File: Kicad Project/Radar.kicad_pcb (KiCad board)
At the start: 2 copper layers, 104.1 x 101.6 mm, 48 parts, among them U1 GALI-1+, U10 GALI-2+, U11 BandpassFilter, U2 MCA1-85L+, U3 BandpassFilter, U4 LMV751, U5 LMV751, U6 GALI-2+, U7 RMK-3-93+, U8 GALI-2+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

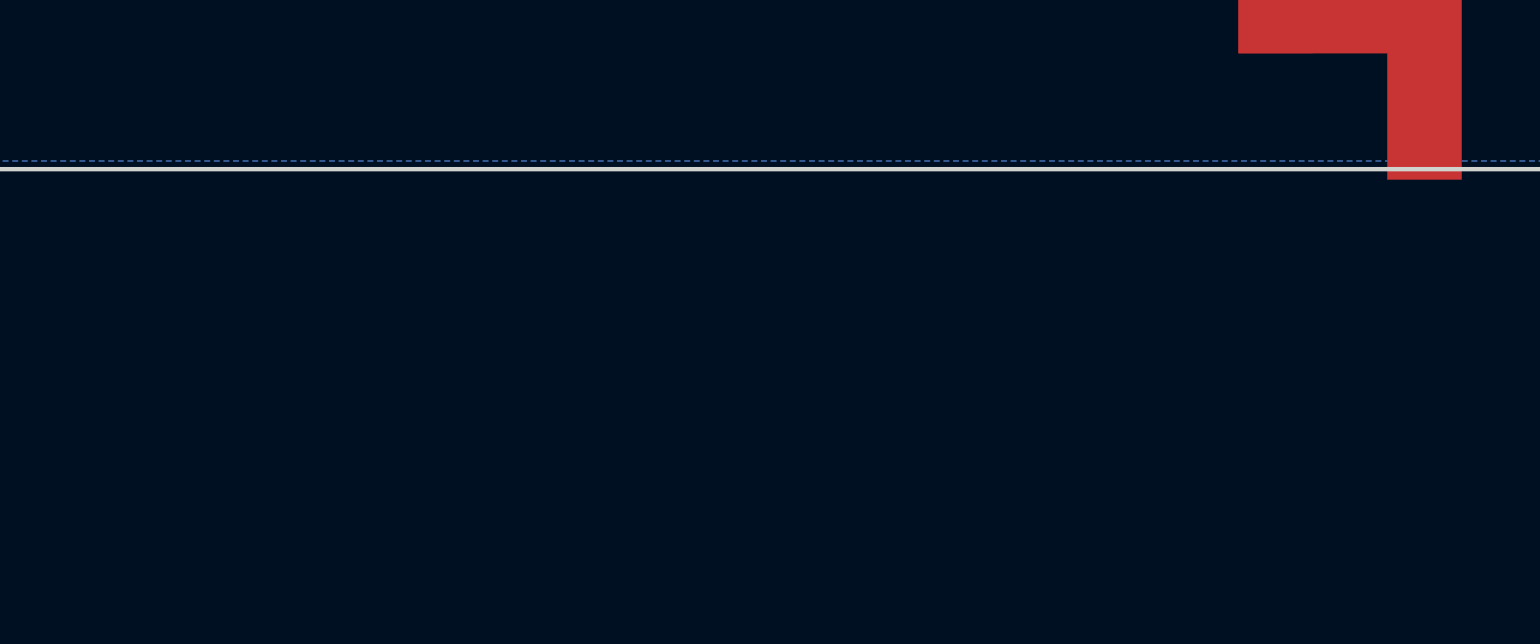
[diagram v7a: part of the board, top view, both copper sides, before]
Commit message: added antennas to pcb
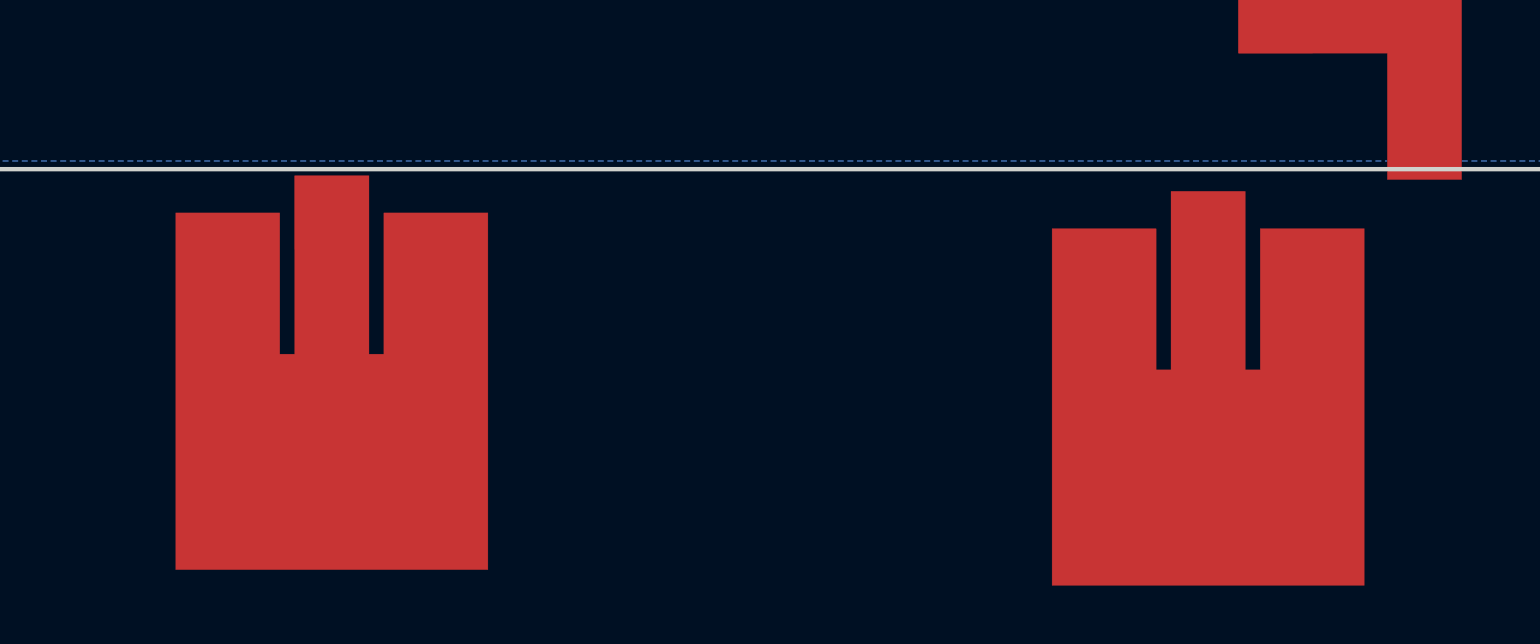
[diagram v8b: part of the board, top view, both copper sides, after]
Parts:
- added U13: Antenna111, RadarComponents:patch58, F.Cu at (116.1, 187.3)
- added U14: Antenna111, RadarComponents:patch58, F.Cu at (146.1, 187.9)
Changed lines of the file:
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@@
     (tracks 61)
     (zones 0)
-    (modules 48)
-    (nets 42)
+    (modules 50)
+    (nets 44)
   )
   (page A4)
@@
   (net 40 "Net-(C4-Pad1)")
   (net 41 "Net-(U3-Pad1)")
+  (net 42 "Net-(U13-Pad1)")
+  (net 43 "Net-(U14-Pad1)")
   (net_class Default "This is the default net class."
     (clearance 0.2)
@@
     (add_net "Net-(R6-Pad2)")
     (add_net "Net-(U11-Pad2)")
+    (add_net "Net-(U13-Pad1)")
+    (add_net "Net-(U14-Pad1)")
     (add_net "Net-(U3-Pad1)")
     (add_net "Net-(VCO1-Pad4)")
@@
       (net 41 "Net-(U3-Pad1)"))
   )
+  (module RadarComponents:patch58 (layer F.Cu)
+    (at 116.1034 187.3377 270)
+    (fp_text reference U13 (at -5.5372 -8.7122 270) (layer F.SilkS) hide
+      (effects (font (thickness 0.3)))
+    )
+    (fp_text value Antenna111 (at 1.0414 -8.636 270) (layer F.SilkS) hide
+      (effects (font (thickness 0.3)))
+    )
+    (fp_poly (pts (xy 4.148667 3.217333) (xy -8.043333 3.217333) (xy -8.043333 -0.338667) (xy -3.217333 -0.338667)
+      (xy -3.217333 -0.846667) (xy -9.313333 -0.846667) (xy -9.313333 -3.386667) (xy -3.217333 -3.386667)
+      (xy -3.217333 -3.894667) (xy -8.043333 -3.894667) (xy -8.043333 -7.450667) (xy 4.148667 -7.450667)
+      (xy 4.148667 3.217333)) (layer F.Cu) (width 0.01))
+    (pad 1 smd rect (at -8.0518 -2.1082 270) (size 2.5146 2.5146) (layers F.Cu F.Paste F.Mask)
+      (net 42 "Net-(U13-Pad1)"))
+  )
+  (module RadarComponents:patch58 (layer F.Cu)
+    (at 146.05 187.875001 270)
+    (fp_text reference U14 (at -5.5372 -8.7122 270) (layer F.SilkS) hide
+      (effects (font (thickness 0.3)))
+    )
+    (fp_text value Antenna111 (at 1.0414 -8.636 270) (layer F.SilkS) hide
+      (effects (font (thickness 0.3)))
+    )
+    (fp_poly (pts (xy 4.148667 3.217333) (xy -8.043333 3.217333) (xy -8.043333 -0.338667) (xy -3.217333 -0.338667)
+      (xy -3.217333 -0.846667) (xy -9.313333 -0.846667) (xy -9.313333 -3.386667) (xy -3.217333 -3.386667)
+      (xy -3.217333 -3.894667) (xy -8.043333 -3.894667) (xy -8.043333 -7.450667) (xy 4.148667 -7.450667)
+      (xy 4.148667 3.217333)) (layer F.Cu) (width 0.01))
+    (pad 1 smd rect (at -8.0518 -2.1082 270) (size 2.5146 2.5146) (layers F.Cu F.Paste F.Mask)
+      (net 43 "Net-(U14-Pad1)"))
+  )
   (gr_line (start 96.52 177.8) (end 93.98 177.8) (angle 90) (layer Edge.Cuts) (width 0.15))
